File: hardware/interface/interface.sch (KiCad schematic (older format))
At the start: 12 parts, among them IC1 ARDUINO NANO, J8 CONN_01X02, Q1 BC547

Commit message: Add PCB for switches and relay.
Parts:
- removed IC1: ARDUINO NANO, symbol ARDUINO_PRO_MINI_5V
- removed J?: LCD, symbol Conn_01x08
- removed RL1: RM50-xx21, symbol RM50-xx21
- removed SW? (x2): TACT-SWITCH, symbol TACT-SWITCH
- added J1: Conn_01x04, Connector_JST:JST_XH_B04B-XH-A_1x04_P2.50mm_Vertical, symbol Connector_Generic:Conn_01x04
- added J2: Conn_01x06, Connector_PinHeader_2.54mm:PinHeader_1x06_P2.54mm_Vertical, symbol Connector_Generic:Conn_01x06
- added R2: R, Resistor_THT:R_Axial_DIN0309_L9.0mm_D3.2mm_P2.54mm_Vertical, symbol Device:R
- added RLY1: RELAY_DIL16, Acs:DIP-16_Relay, symbol w_relay:RELAY_DIL16
- C2: footprint (none) -> Capacitor_THT:CP_Radial_D10.0mm_P5.00mm; symbol C -> interface-rescue:C
- D1: footprint (none) -> Diode_THT:D_DO-35_SOD27_P2.54mm_Vertical_AnodeUp; symbol DIODE -> interface-rescue:DIODE
- J8: footprint (none) -> Connector_JST:JST_XH_B02B-XH-A_1x02_P2.50mm_Vertical; symbol CONN_01X02 -> interface-rescue:CONN_01X02
- Q1: footprint TO_SOT_Packages_THT:TO-92_Molded_Narrow -> Package_TO_SOT_THT:TO-92; symbol BC547 -> interface-rescue:BC547
- R1, R3: renamed from R?; footprint (none) -> Resistor_THT:R_Axial_DIN0309_L9.0mm_D3.2mm_P2.54mm_Vertical; symbol R -> Device:R
- R4: renamed from R2; footprint (none) -> Resistor_THT:R_Axial_DIN0309_L9.0mm_D3.2mm_P5.08mm_Vertical; symbol R -> Device:R
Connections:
- net labels removed: +12V, +5V, D10, D11, D13, D5, D6, D7, D8, D9
- wire segments 57 -> 48
- no-connect marks 21 -> 1

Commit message: Update.
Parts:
- added H1, H2, H3, H4: MountingHole, MountingHole:MountingHole_2.7mm_M2.5, symbol Mechanical:MountingHole
- added R4: 1K, Resistor_THT:R_Axial_DIN0309_L9.0mm_D3.2mm_P5.08mm_Vertical, symbol Device:R
- J1: value Conn_01x04 -> Switches
- J2: value Conn_01x06 -> Arduino; footprint Connector_PinHeader_2.54mm:PinHeader_1x06_P2.54mm_Vertical -> Connector_PinHeader_2.54mm:PinHeader_1x04_P2.54mm_Vertical; symbol Connector_Generic:Conn_01x06 -> Connector_Generic:Conn_01x04
- J8: symbol interface-rescue:CONN_01X02 -> Connector_Generic:Conn_01x02
- Q1: footprint Package_TO_SOT_THT:TO-92 -> Package_TO_SOT_THT:TO-92_Wide
- R1: value R -> 1K; footprint Resistor_THT:R_Axial_DIN0309_L9.0mm_D3.2mm_P2.54mm_Vertical -> Resistor_THT:R_Axial_DIN0309_L9.0mm_D3.2mm_P5.08mm_Vertical
- R2: value R -> 2K2; footprint Resistor_THT:R_Axial_DIN0309_L9.0mm_D3.2mm_P2.54mm_Vertical -> Resistor_THT:R_Axial_DIN0309_L9.0mm_D3.2mm_P5.08mm_Vertical
- R3: value R -> 5K1; footprint Resistor_THT:R_Axial_DIN0309_L9.0mm_D3.2mm_P2.54mm_Vertical -> Resistor_THT:R_Axial_DIN0309_L9.0mm_D3.2mm_P5.08mm_Vertical
- renumbered R4 to R5
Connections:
- wire segments 48 -> 47
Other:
- note added: "+5V"
- note added: "GND"
- note added: "RELAY (D12)"
- note added: "SW1 (A5)"
- moved on the sheet: R1, R2, R3
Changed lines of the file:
@@
 F 0 "Q1" H 7700 5075 50  0000 L CNN
 F 1 "BC547" H 7700 5000 50  0000 L CNN
-F 2 "Package_TO_SOT_THT:TO-92" H 7700 4925 50  0001 L CIN
+F 2 "Package_TO_SOT_THT:TO-92_Wide" H 7700 4925 50  0001 L CIN
 F 3 "" H 7500 5000 50  0001 L CNN
 	1    7500 5000
@@
 Connection ~ 7050 4000
 $Comp
-L interface-rescue:CONN_01X02 J8
+L Connector_Generic:Conn_01x02 J8
 U 1 1 58D2EE7D
-P 9150 4450
-F 0 "J8" H 9150 4600 50  0000 C CNN
-F 1 "CONN_01X02" V 9250 4450 50  0000 C CNN
-F 2 "Connector_JST:JST_XH_B02B-XH-A_1x02_P2.50mm_Vertical" H 9150 4450 50  0001 C CNN
-F 3 "" H 9150 4450 50  0001 C CNN
-	1    9150 4450
-	1    0    0    -1
-$EndComp
-Wire Wire Line
-	7900 4200 7900 4050
-Wire Wire Line
-	7900 4050 8800 4050
+P 9150 4400
+F 0 "J8" H 9150 4550 50  0000 C CNN
+F 1 "CONN_01X02" V 9250 4400 50  0000 C CNN
+F 2 "Connector_JST:JST_XH_B02B-XH-A_1x02_P2.50mm_Vertical" H 9150 4400 50  0001 C CNN
+F 3 "" H 9150 4400 50  0001 C CNN
+	1    9150 4400
+	1    0    0    -1
+$EndComp
 Wire Wire Line
 	8800 4050 8800 4400
@@
 Wire Wire Line
 	8800 4500 8800 4800
-Wire Wire Line
-	8800 4800 7850 4800
-Wire Wire Line
-	7850 4800 7850 4600
 Text Notes 9350 4500 0    60   ~ 0
 LATCH
@@
 L Device:R R1
 U 1 1 598071E6
-P 2950 2450
-F 0 "R1" V 3030 2450 50  0000 C CNN
-F 1 "R" V 2950 2450 50  0000 C CNN
-F 2 "Resistor_THT:R_Axial_DIN0309_L9.0mm_D3.2mm_P2.54mm_Vertical" V 2880 2450 50  0001 C CNN
-F 3 "" H 2950 2450 50  0001 C CNN
-	1    2950 2450
-	1    0    0    -1
+P 2750 3200
+F 0 "R1" V 2700 3050 50  0000 C CNN
+F 1 "1K" V 2750 3200 50  0000 C CNN
+F 2 "Resistor_THT:R_Axial_DIN0309_L9.0mm_D3.2mm_P5.08mm_Vertical" V 2680 3200 50  0001 C CNN
+F 3 "" H 2750 3200 50  0001 C CNN
+	1    2750 3200
+	0    1    1    0
 $EndComp
 $Comp
 L Device:R R3
 U 1 1 5980722B
-P 3900 2450
-F 0 "R3" V 3980 2450 50  0000 C CNN
-F 1 "R" V 3900 2450 50  0000 C CNN
-F 2 "Resistor_THT:R_Axial_DIN0309_L9.0mm_D3.2mm_P2.54mm_Vertical" V 3830 2450 50  0001 C CNN
-F 3 "" H 3900 2450 50  0001 C CNN
-	1    3900 2450
-	1    0    0    -1
+P 2750 3400
+F 0 "R3" V 2700 3250 50  0000 C CNN
+F 1 "5K1" V 2750 3400 50  0000 C CNN
+F 2 "Resistor_THT:R_Axial_DIN0309_L9.0mm_D3.2mm_P5.08mm_Vertical" V 2680 3400 50  0001 C CNN
+F 3 "" H 2750 3400 50  0001 C CNN
+	1    2750 3400
+	0    1    1    0
 $EndComp
 $Comp
@@
 $EndComp
 Wire Wire Line
-	2950 2200 3450 2200
-Wire Wire Line
-	3900 2200 3900 2300
-Wire Wire Line
 	6650 4000 7050 4000
 $Comp
@@
 	7050 4000 7600 4000
 Wire Wire Line
-	2950 2200 2950 2300
-Wire Wire Line
 	7600 5250 7600 5200
 $Comp
@@
 P 2300 3400
 F 0 "J1" H 2218 2975 50  0000 C CNN
-F 1 "Conn_01x04" H 2218 3066 50  0000 C CNN
+F 1 "Switches" H 2218 3066 50  0000 C CNN
 F 2 "Connector_JST:JST_XH_B04B-XH-A_1x04_P2.50mm_Vertical" H 2300 3400 50  0001 C CNN
 F 3 "~" H 2300 3400 50  0001 C CNN
@@
 Wire Wire Line
 	2950 3500 2950 3900
-Wire Wire Line
-	2950 3200 2500 3200
 $Comp
 L Device:R R2
 U 1 1 5CE009C8
-P 3450 2450
-F 0 "R2" H 3520 2496 50  0000 L CNN
-F 1 "R" H 3520 2405 50  0000 L CNN
-F 2 "Resistor_THT:R_Axial_DIN0309_L9.0mm_D3.2mm_P2.54mm_Vertical" V 3380 2450 50  0001 C CNN
-F 3 "~" H 3450 2450 50  0001 C CNN
-	1    3450 2450
-	1    0    0    -1
-$EndComp
-Wire Wire Line
-	3450 2200 3450 2300
-Connection ~ 3450 2200
-Wire Wire Line
-	3450 2200 3900 2200
-Wire Wire Line
-	3450 3300 2500 3300
-Wire Wire Line
-	2500 3400 3900 3400
-Wire Wire Line
-	4100 3400 3900 3400
-Connection ~ 3900 3400
-Wire Wire Line
-	3900 2600 3900 3400
-Wire Wire Line
-	3450 2600 3450 3300
-Wire Wire Line
-	2950 2600 2950 3200
-Wire Wire Line
-	4100 3300 3450 3300
-Connection ~ 3450 3300
-Wire Wire Line
-	4100 3200 2950 3200
-Connection ~ 2950 3200
-Wire Wire Line
-	4100 3500 2950 3500
-Connection ~ 2950 3500
+P 2750 3300
+F 0 "R2" V 2700 3100 50  0000 L CNN
+F 1 "2K2" V 2750 3300 50  0000 C CNN
+F 2 "Resistor_THT:R_Axial_DIN0309_L9.0mm_D3.2mm_P5.08mm_Vertical" V 2680 3300 50  0001 C CNN
+F 3 "~" H 2750 3300 50  0001 C CNN
+	1    2750 3300
+	0    1    1    0
+$EndComp
 Wire Wire Line
 	4100 3100 4050 3100
@@
 	4050 5000 6700 5000
 $Comp
-L Device:R R4
+L Device:R R5
 U 1 1 58D2EA0D
 P 6850 5000
-F 0 "R4" V 6930 5000 50  0000 C CNN
+F 0 "R5" V 6930 5000 50  0000 C CNN
 F 1 "1K" V 6850 5000 50  0000 C CNN
 F 2 "Resistor_THT:R_Axial_DIN0309_L9.0mm_D3.2mm_P5.08mm_Vertical" V 6780 5000 50  0001 C CNN
@@
 $EndComp
 $Comp
-L Connector_Generic:Conn_01x06 J2
+L Connector_Generic:Conn_01x04 J2
 U 1 1 5CE0A21E
-P 4300 3200
-F 0 "J2" H 4380 3192 50  0000 L CNN
-F 1 "Conn_01x06" H 4380 3101 50  0000 L CNN
-F 2 "Connector_PinHeader_2.54mm:PinHeader_1x06_P2.54mm_Vertical" H 4300 3200 50  0001 C CNN
-F 3 "~" H 4300 3200 50  0001 C CNN
-	1    4300 3200
+P 4300 3100
+F 0 "J2" H 4250 2650 50  0000 L CNN
+F 1 "Arduino" H 4250 2550 50  0000 L CNN
+F 2 "Connector_PinHeader_2.54mm:PinHeader_1x04_P2.54mm_Vertical" H 4300 3100 50  0001 C CNN
+F 3 "~" H 4300 3100 50  0001 C CNN
+	1    4300 3100
 	1    0    0    -1
 $EndComp
@@
 F 3 "" H 7750 4400 60  0000 C CNN
 	1    7750 4400
-	0    -1   -1   0
+	0    -1   1    0
 $EndComp
 Wire Wire Line
@@
 	7600 4600 7600 4750
 Wire Wire Line
-	3900 2200 7050 2200
-Wire Wire Line
 	7050 2200 7050 2850
-Connection ~ 3900 2200
 Connection ~ 7050 2850
+Wire Wire Line
+	7900 4600 7900 4800
+Wire Wire Line
+	7900 4800 8800 4800
+Wire Wire Line
+	7850 4050 7850 4200
+Wire Wire Line
+	7850 4050 8800 4050
+$Comp
+L Mechanical:MountingHole H1
+U 1 1 5CE975F5
+P 1650 5300
+F 0 "H1" H 1750 5346 50  0000 L CNN
+F 1 "MountingHole" H 1750 5255 50  0000 L CNN
+F 2 "MountingHole:MountingHole_2.7mm_M2.5" H 1650 5300 50  0001 C CNN
+F 3 "~" H 1650 5300 50  0001 C CNN
+	1    1650 5300
+	1    0    0    -1
+$EndComp
+$Comp
+L Mechanical:MountingHole H2
+U 1 1 5CE979F8
+P 1650 5700
+F 0 "H2" H 1750 5746 50  0000 L CNN
+F 1 "MountingHole" H 1750 5655 50  0000 L CNN
+F 2 "MountingHole:MountingHole_2.7mm_M2.5" H 1650 5700 50  0001 C CNN
+F 3 "~" H 1650 5700 50  0001 C CNN
+	1    1650 5700
+	1    0    0    -1
+$EndComp
+$Comp
+L Mechanical:MountingHole H3
+U 1 1 5CE97D65
+P 1650 6050
+F 0 "H3" H 1750 6096 50  0000 L CNN
+F 1 "MountingHole" H 1750 6005 50  0000 L CNN
+F 2 "MountingHole:MountingHole_2.7mm_M2.5" H 1650 6050 50  0001 C CNN
+F 3 "~" H 1650 6050 50  0001 C CNN
+	1    1650 6050
+	1    0    0    -1
+$EndComp
+$Comp
+L Mechanical:MountingHole H4
+U 1 1 5CE9804D
+P 1650 6400
+F 0 "H4" H 1750 6446 50  0000 L CNN
+F 1 "MountingHole" H 1750 6355 50  0000 L CNN
+F 2 "MountingHole:MountingHole_2.7mm_M2.5" H 1650 6400 50  0001 C CNN
+F 3 "~" H 1650 6400 50  0001 C CNN
+	1    1650 6400
+	1    0    0    -1
+$EndComp
+Text Notes 4400 3350 0    60   ~ 0
+GND
+Text Notes 4400 3050 0    60   ~ 0
++5V
+Text Notes 4400 3150 0    60   ~ 0
+RELAY (D12)
+Text Notes 4400 3250 0    60   ~ 0
+SW1 (A5)
+Wire Wire Line
+	4100 3300 3700 3300
+Wire Wire Line
+	3700 3300 3700 3500
+Wire Wire Line
+	3700 3500 2950 3500
+Connection ~ 2950 3500
+Wire Wire Line
+	2500 3200 2600 3200
+Wire Wire Line
+	2600 3300 2500 3300
+Wire Wire Line
+	2500 3400 2600 3400
+Wire Wire Line
+	2950 2200 7050 2200
+Wire Wire Line
+	2950 2200 2950 2750
+Wire Wire Line
+	2950 3050 2950 3200
+Wire Wire Line
+	2950 3400 2900 3400
+Wire Wire Line
+	2900 3300 2950 3300
+Connection ~ 2950 3300
+Wire Wire Line
+	2950 3300 2950 3400
+Wire Wire Line
+	2900 3200 2950 3200
+Connection ~ 2950 3200
+Wire Wire Line
+	2950 3200 2950 3300
+Wire Wire Line
+	2950 3200 4100 3200
+$Comp
+L Device:R R4
+U 1 1 5CEB36BC
+P 2950 2900
+F 0 "R4" H 3020 2946 50  0000 L CNN
+F 1 "1K" H 3020 2855 50  0000 L CNN
+F 2 "Resistor_THT:R_Axial_DIN0309_L9.0mm_D3.2mm_P5.08mm_Vertical" V 2880 2900 50  0001 C CNN
+F 3 "~" H 2950 2900 50  0001 C CNN
+	1    2950 2900
+	1    0    0    -1
+$EndComp
 $EndSCHEMATC

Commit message: Add filter resistor on supply line.
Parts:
- added R?: 20, symbol Device:R
- H1, H2, H3, H4: symbol Mechanical:MountingHole -> interface-rescue:MountingHole-Mechanical
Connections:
- net at C2.1, D1.2 (K), R4.1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: now also R?.1; no longer J2.1 (Pin_1)
- new net: J2.1 (Pin_1), R?.2
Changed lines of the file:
@@
 EESchema Schematic File Version 4
-LIBS:interface-cache
-EELAYER 29 0
+EELAYER 30 0
 EELAYER END
 $Descr A4 11693 8268
@@
 Wire Wire Line
 	4050 3000 4050 2850
-Wire Wire Line
-	4050 2850 7050 2850
-Wire Wire Line
-	7050 2850 7050 4000
 $Comp
 L w_relay:RELAY_DIL16 RLY1
@@
 	7600 4600 7600 4750
 Wire Wire Line
-	7050 2200 7050 2850
-Connection ~ 7050 2850
-Wire Wire Line
 	7900 4600 7900 4800
 Wire Wire Line
@@
 	7850 4050 8800 4050
 $Comp
-L Mechanical:MountingHole H1
+L interface-rescue:MountingHole-Mechanical H1
 U 1 1 5CE975F5
 P 1650 5300
@@
 $EndComp
 $Comp
-L Mechanical:MountingHole H2
+L interface-rescue:MountingHole-Mechanical H2
 U 1 1 5CE979F8
 P 1650 5700
@@
 $EndComp
 $Comp
-L Mechanical:MountingHole H3
+L interface-rescue:MountingHole-Mechanical H3
 U 1 1 5CE97D65
 P 1650 6050
@@
 $EndComp
 $Comp
-L Mechanical:MountingHole H4
+L interface-rescue:MountingHole-Mechanical H4
 U 1 1 5CE9804D
 P 1650 6400
@@
 	1    0    0    -1
 $EndComp
+Wire Wire Line
+	7050 2200 7050 2850
+$Comp
+L Device:R R?
+U 1 1 60566F03
+P 5075 2850
+F 0 "R?" V 4868 2850 50  0000 C CNN
+F 1 "20" V 4959 2850 50  0000 C CNN
+F 2 "" V 5005 2850 50  0001 C CNN
+F 3 "~" H 5075 2850 50  0001 C CNN
+	1    5075 2850
+	0    1    1    0
+$EndComp
+Wire Wire Line
+	4925 2850 4050 2850
+Wire Wire Line
+	5225 2850 7050 2850
+Connection ~ 7050 2850
+Wire Wire Line
+	7050 2850 7050 4000
 $EndSCHEMATC

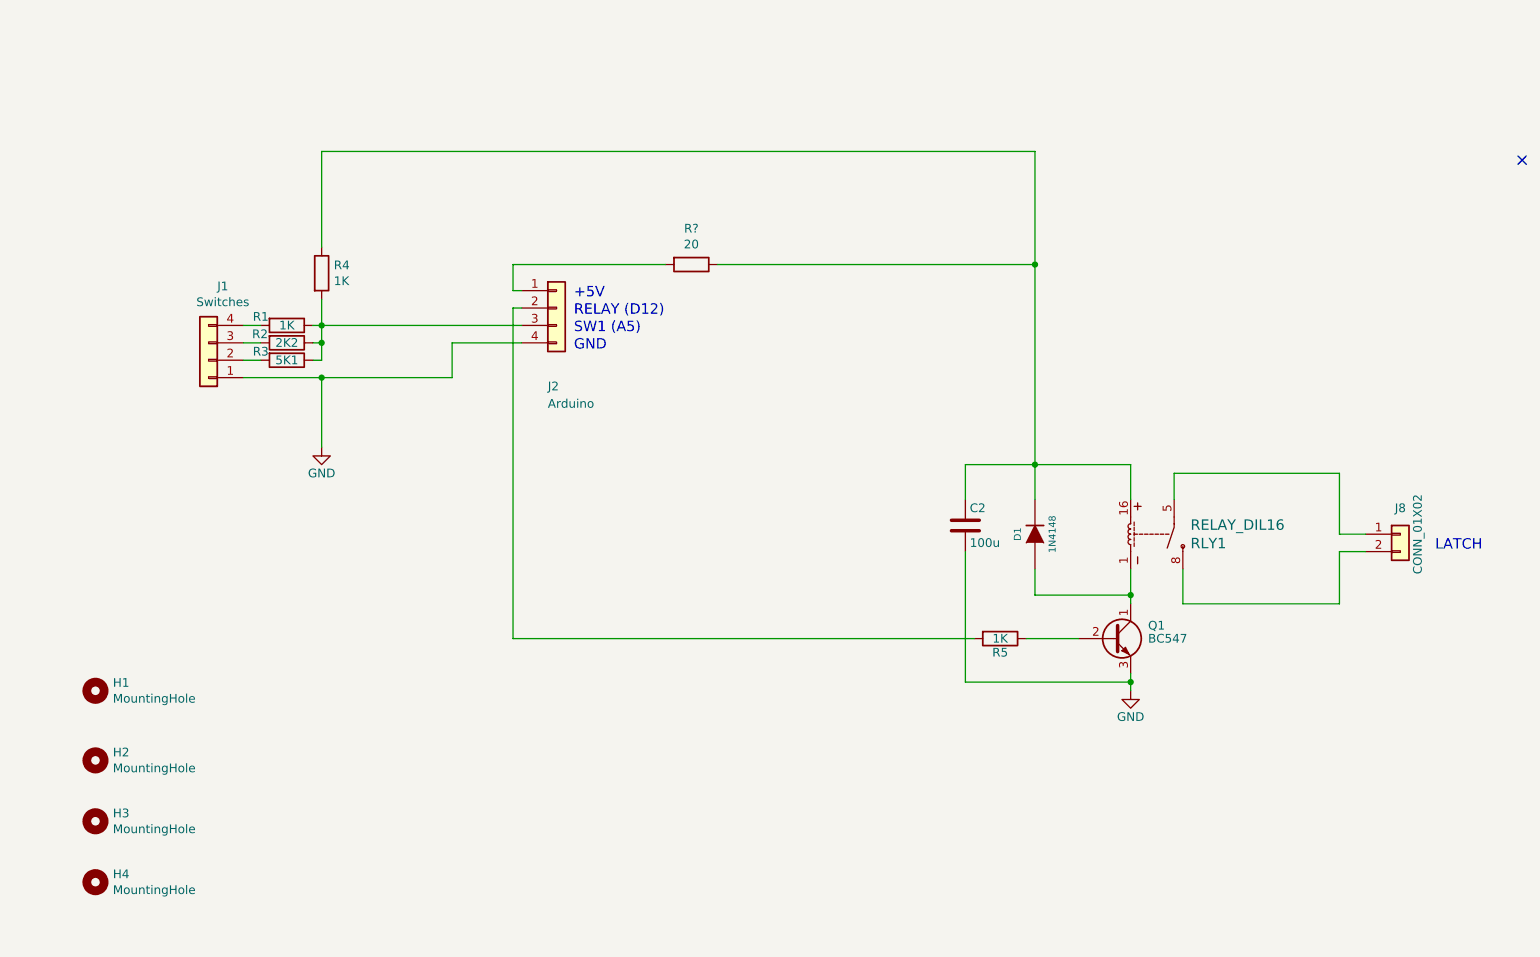
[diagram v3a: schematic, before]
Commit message: Replace relay with button 4.
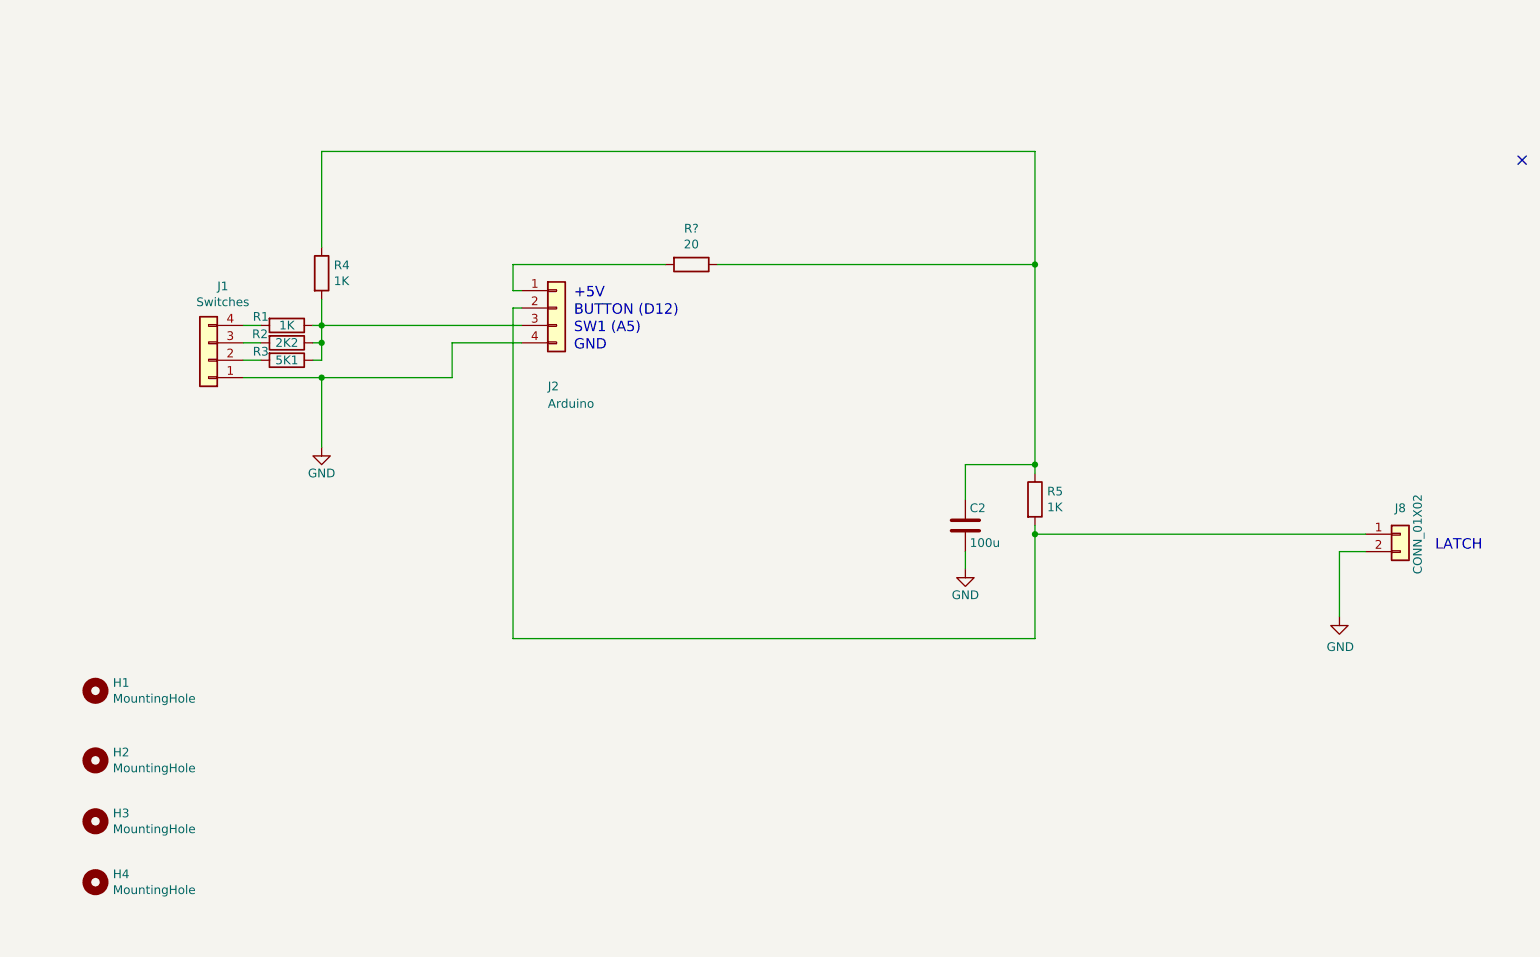
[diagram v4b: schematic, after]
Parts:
- removed D1: 1N4148, Diode_THT:D_DO-35_SOD27_P2.54mm_Vertical_AnodeUp, symbol interface-rescue:DIODE
- removed Q1: BC547, Package_TO_SOT_THT:TO-92_Wide, symbol interface-rescue:BC547
- removed RLY1: RELAY_DIL16, Acs:DIP-16_Relay, symbol w_relay:RELAY_DIL16
- R5: footprint Resistor_THT:R_Axial_DIN0309_L9.0mm_D3.2mm_P5.08mm_Vertical -> (none)
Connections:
- net GND: now also J8.2 (Pin_2)
- net at R5.1: now also C2.1, R4.1, R?.1
- net at J2.2 (Pin_2), R5.2: now also J8.1 (Pin_1)
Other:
- note added: "BUTTON (D12)"
- note removed: "RELAY (D12)"
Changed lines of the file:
@@
 $EndDescr
-$Comp
-L interface-rescue:BC547 Q1
-U 1 1 58D2E8F5
-P 7500 5000
-F 0 "Q1" H 7700 5075 50  0000 L CNN
-F 1 "BC547" H 7700 5000 50  0000 L CNN
-F 2 "Package_TO_SOT_THT:TO-92_Wide" H 7700 4925 50  0001 L CIN
-F 3 "" H 7500 5000 50  0001 L CNN
-	1    7500 5000
-	1    0    0    -1
-$EndComp
-$Comp
-L interface-rescue:DIODE D1
-U 1 1 58D2E9AA
-P 7050 4400
-F 0 "D1" H 7050 4500 40  0000 C CNN
-F 1 "1N4148" H 7050 4300 40  0000 C CNN
-F 2 "Diode_THT:D_DO-35_SOD27_P2.54mm_Vertical_AnodeUp" H 7050 4400 60  0001 C CNN
-F 3 "" H 7050 4400 60  0000 C CNN
-	1    7050 4400
-	0    -1   -1   0
-$EndComp
-Wire Wire Line
-	7000 5000 7300 5000
 $Comp
 L interface-rescue:GND #PWR014
 U 1 1 58D2EBAA
-P 7600 5300
-F 0 "#PWR014" H 7600 5050 50  0001 C CNN
-F 1 "GND" H 7600 5150 50  0000 C CNN
-F 2 "" H 7600 5300 50  0001 C CNN
-F 3 "" H 7600 5300 50  0001 C CNN
-	1    7600 5300
-	1    0    0    -1
-$EndComp
-Wire Wire Line
-	7600 5300 7600 5250
-Wire Wire Line
-	7050 4600 7050 4750
-Wire Wire Line
-	7050 4750 7600 4750
-Connection ~ 7600 4750
+P 6650 4600
+F 0 "#PWR014" H 6650 4350 50  0001 C CNN
+F 1 "GND" H 6650 4450 50  0000 C CNN
+F 2 "" H 6650 4600 50  0001 C CNN
+F 3 "" H 6650 4600 50  0001 C CNN
+	1    6650 4600
+	1    0    0    -1
+$EndComp
 Connection ~ 7050 4000
 $Comp
@@
 $EndComp
 Wire Wire Line
-	8800 4050 8800 4400
-Wire Wire Line
-	8800 4400 8950 4400
-Wire Wire Line
 	8950 4500 8800 4500
-Wire Wire Line
-	8800 4500 8800 4800
 Text Notes 9350 4500 0    60   ~ 0
 LATCH
@@
 Wire Wire Line
 	6650 4000 6650 4200
-Wire Wire Line
-	6650 4500 6650 5250
-Wire Wire Line
-	6650 5250 7600 5250
-Connection ~ 7600 5250
-Wire Wire Line
-	7600 4750 7600 4800
-Wire Wire Line
-	7050 4000 7050 4200
-Wire Wire Line
-	7050 4000 7600 4000
-Wire Wire Line
-	7600 5250 7600 5200
 $Comp
 L Connector_Generic:Conn_01x04 J1
@@
 Wire Wire Line
 	4050 3100 4050 5000
-Wire Wire Line
-	4050 5000 6700 5000
-$Comp
-L Device:R R5
-U 1 1 58D2EA0D
-P 6850 5000
-F 0 "R5" V 6930 5000 50  0000 C CNN
-F 1 "1K" V 6850 5000 50  0000 C CNN
-F 2 "Resistor_THT:R_Axial_DIN0309_L9.0mm_D3.2mm_P5.08mm_Vertical" V 6780 5000 50  0001 C CNN
-F 3 "" H 6850 5000 50  0001 C CNN
-	1    6850 5000
-	0    1    1    0
-$EndComp
 $Comp
 L Connector_Generic:Conn_01x04 J2
@@
 	4050 3000 4050 2850
 $Comp
-L w_relay:RELAY_DIL16 RLY1
-U 1 1 5CE10714
-P 7750 4400
-F 0 "RLY1" V 7803 4206 60  0000 R CNN
-F 1 "RELAY_DIL16" V 7697 4206 60  0000 R CNN
-F 2 "Acs:DIP-16_Relay" H 7750 4400 60  0001 C CNN
-F 3 "" H 7750 4400 60  0000 C CNN
-	1    7750 4400
-	0    -1   1    0
-$EndComp
-Wire Wire Line
-	7600 4000 7600 4200
-Wire Wire Line
-	7600 4600 7600 4750
-Wire Wire Line
-	7900 4600 7900 4800
-Wire Wire Line
-	7900 4800 8800 4800
-Wire Wire Line
-	7850 4050 7850 4200
-Wire Wire Line
-	7850 4050 8800 4050
-$Comp
 L interface-rescue:MountingHole-Mechanical H1
 U 1 1 5CE975F5
@@
 +5V
 Text Notes 4400 3150 0    60   ~ 0
-RELAY (D12)
+BUTTON (D12)
 Text Notes 4400 3250 0    60   ~ 0
 SW1 (A5)
@@
 Wire Wire Line
 	7050 2850 7050 4000
+$Comp
+L Device:R R5
+U 1 1 6060E0D3
+P 7050 4200
+F 0 "R5" H 7120 4246 50  0000 L CNN
+F 1 "1K" H 7120 4155 50  0000 L CNN
+F 2 "" V 6980 4200 50  0001 C CNN
+F 3 "~" H 7050 4200 50  0001 C CNN
+	1    7050 4200
+	1    0    0    -1
+$EndComp
+Wire Wire Line
+	7050 4400 7050 4350
+Wire Wire Line
+	7050 4400 8950 4400
+Wire Wire Line
+	7050 4050 7050 4000
+$Comp
+L interface-rescue:GND #PWR?
+U 1 1 6061156C
+P 8800 4875
+F 0 "#PWR?" H 8800 4625 50  0001 C CNN
+F 1 "GND" H 8805 4702 50  0000 C CNN
+F 2 "" H 8800 4875 50  0001 C CNN
+F 3 "" H 8800 4875 50  0001 C CNN
+	1    8800 4875
+	1    0    0    -1
+$EndComp
+Wire Wire Line
+	8800 4500 8800 4875
+Wire Wire Line
+	7050 4400 7050 5000
+Wire Wire Line
+	4050 5000 7050 5000
+Connection ~ 7050 4400
+Wire Wire Line
+	6650 4500 6650 4600
 $EndSCHEMATC
